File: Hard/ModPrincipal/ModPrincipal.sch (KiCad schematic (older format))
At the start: 0 parts

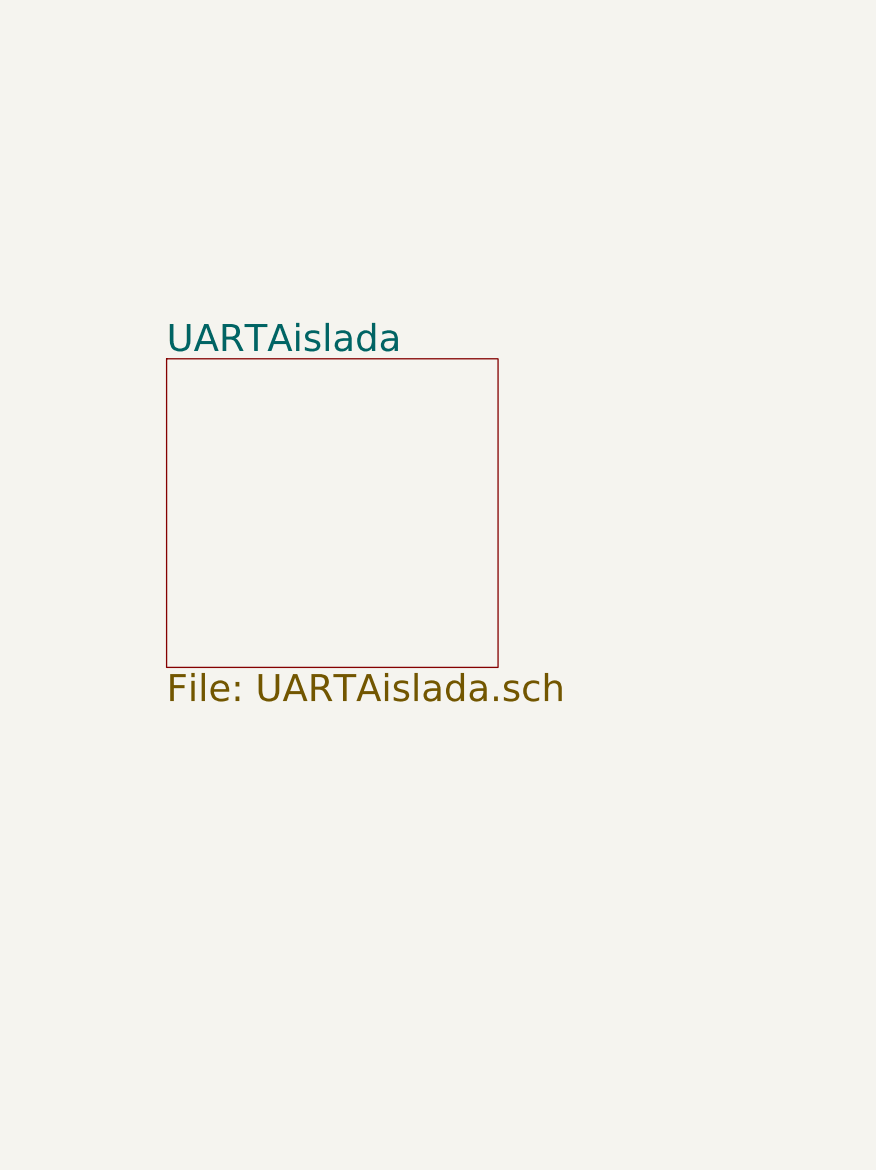
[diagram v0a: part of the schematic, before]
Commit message: Agrego UART aislada y salidas digitales
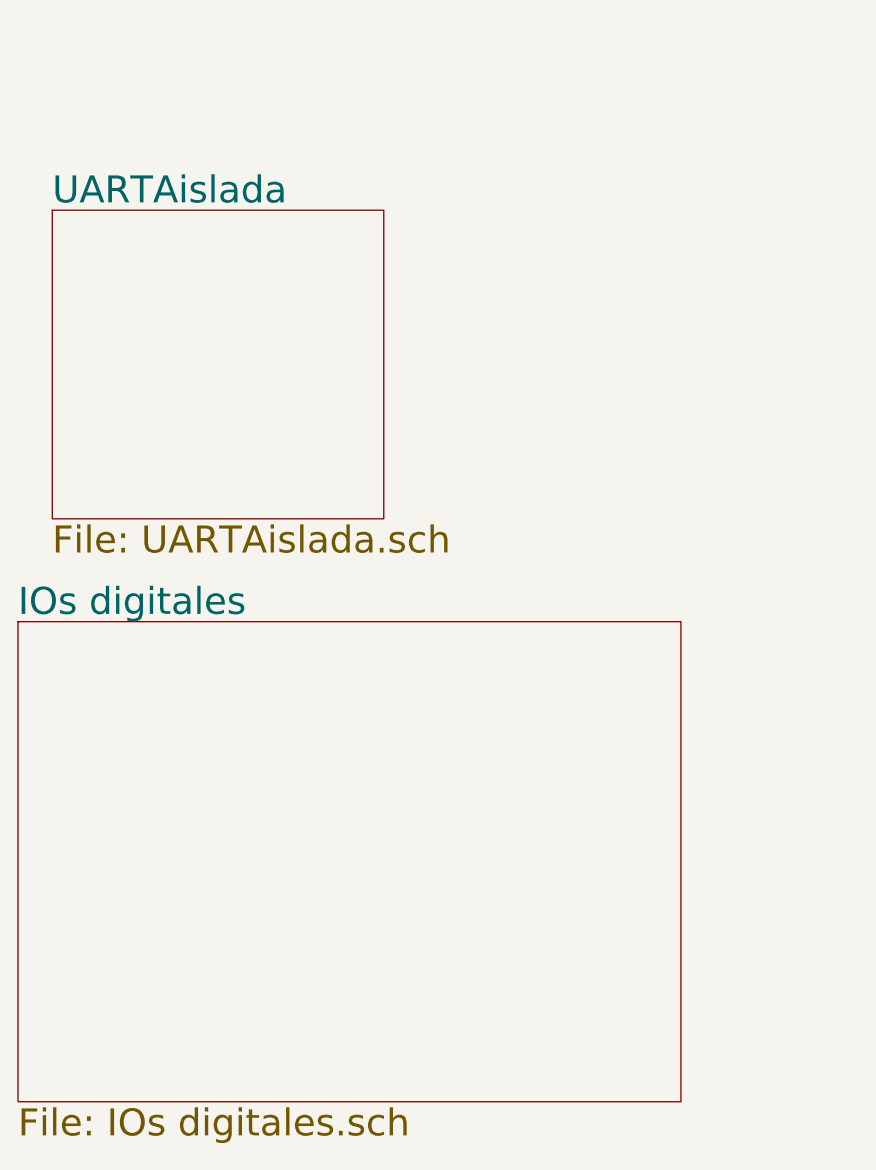
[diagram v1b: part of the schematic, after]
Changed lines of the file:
@@
 EESchema Schematic File Version 4
-LIBS:ModPrincipal-cache
 EELAYER 30 0
 EELAYER END
 $Descr A4 11693 8268
 encoding utf-8
-Sheet 1 4
+Sheet 1 5
 Title ""
 Date ""
@@
 $EndSheet
 $Sheet
-S 2150 4100 1450 1350
+S 1650 3450 1450 1350
 U 5ED20EE2
 F0 "UARTAislada" 118
 F1 "UARTAislada.sch" 118
 $EndSheet
+$Sheet
+S 1500 5250 2900 2100
+U 5EE6B2B0
+F0 "IOs digitales" 118
+F1 "IOs digitales.sch" 118
+$EndSheet
 $EndSCHEMATC

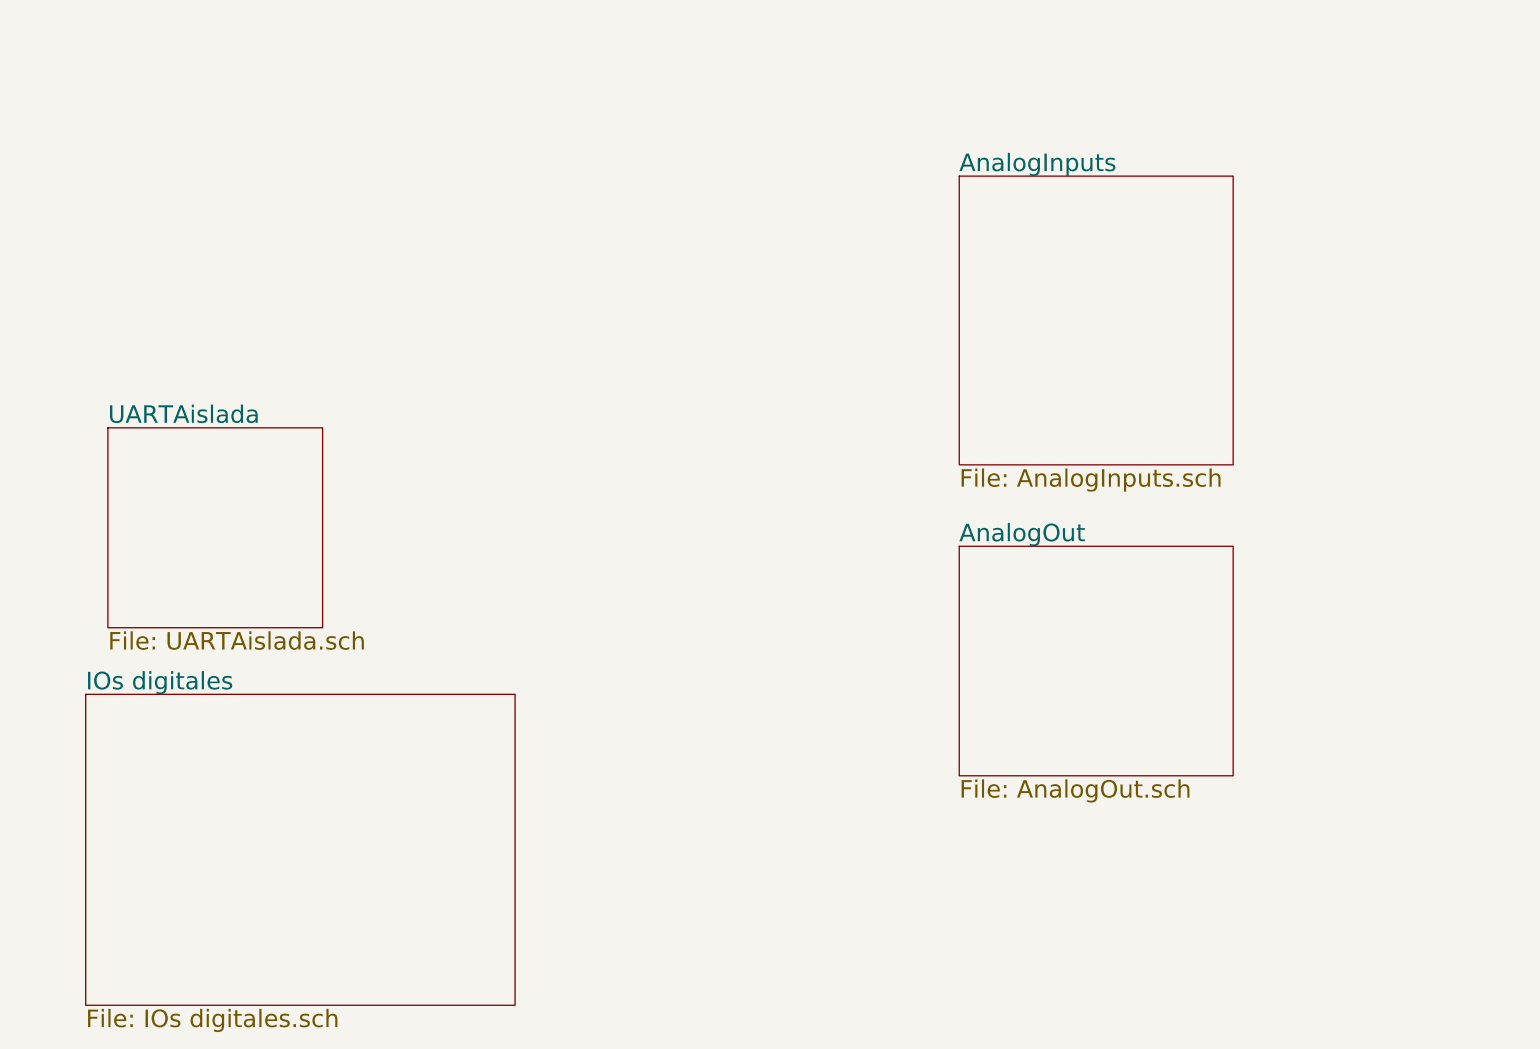
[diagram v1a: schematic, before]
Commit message: Agrego fuente de alimentación
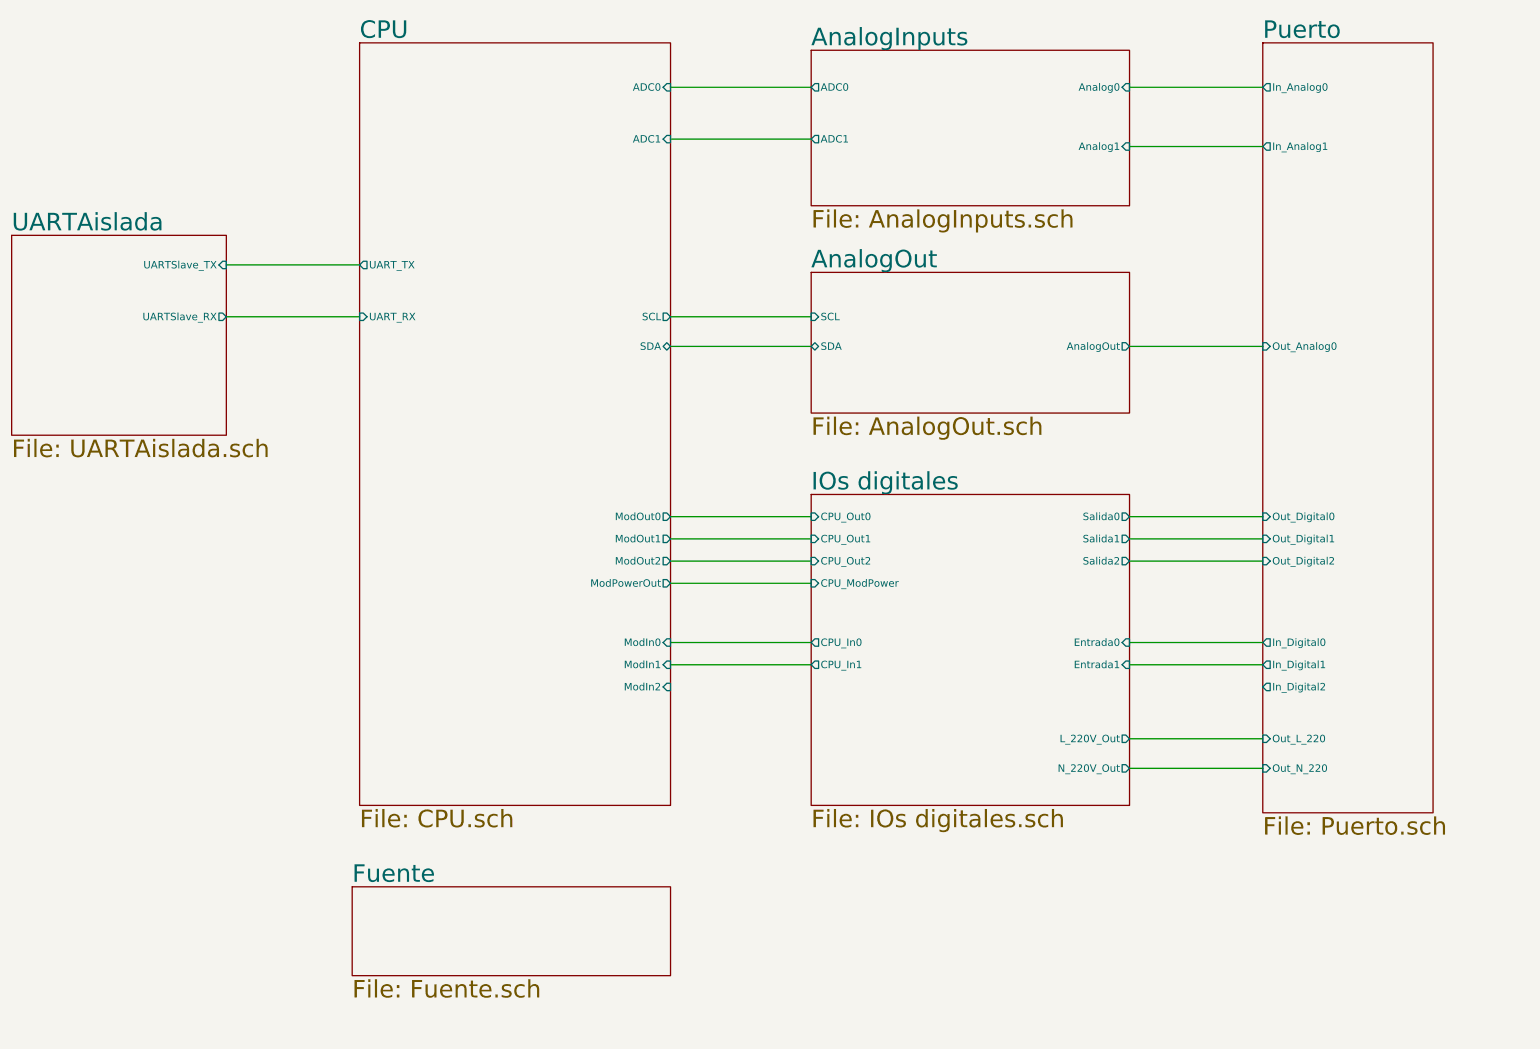
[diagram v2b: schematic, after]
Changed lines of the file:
@@
 $Descr A4 11693 8268
 encoding utf-8
-Sheet 1 5
+Sheet 1 8
 Title ""
 Date ""
@@
 $EndDescr
 $Sheet
-S 7400 1750 1850 1950
+S 6400 900  2150 1050
 U 5EC7150D
 F0 "AnalogInputs" 118
 F1 "AnalogInputs.sch" 118
+F2 "Analog0" I R 8550 1150 50
+F3 "Analog1" I R 8550 1550 50
+F4 "ADC0" O L 6400 1150 50
+F5 "ADC1" O L 6400 1500 50
 $EndSheet
 $Sheet
-S 7400 4250 1850 1550
+S 6400 2400 2150 950
 U 5ECD8445
 F0 "AnalogOut" 118
 F1 "AnalogOut.sch" 118
+F2 "AnalogOut" O R 8550 2900 50
+F3 "SDA" B L 6400 2900 50
+F4 "SCL" I L 6400 2700 50
 $EndSheet
 $Sheet
-S 1650 3450 1450 1350
+S 1000 2150 1450 1350
 U 5ED20EE2
 F0 "UARTAislada" 118
 F1 "UARTAislada.sch" 118
+F2 "UARTSlave_TX" I R 2450 2350 50
+F3 "UARTSlave_RX" O R 2450 2700 50
 $EndSheet
 $Sheet
-S 1500 5250 2900 2100
+S 3300 6550 2150 600
+U 5ECEE31C
+F0 "Fuente" 118
+F1 "Fuente.sch" 118
+$EndSheet
+Wire Wire Line
+	3350 2350 2450 2350
+Wire Wire Line
+	2450 2700 3350 2700
+$Sheet
+S 9450 850  1150 5200
+U 5EE56CB1
+F0 "Puerto" 118
+F1 "Puerto.sch" 118
+F2 "Out_Digital1" I L 9450 4200 50
+F3 "Out_Digital2" I L 9450 4350 50
+F4 "Out_Digital0" I L 9450 4050 50
+F5 "In_Digital1" O L 9450 5050 50
+F6 "In_Digital2" O L 9450 5200 50
+F7 "In_Digital0" O L 9450 4900 50
+F8 "Out_Analog0" I L 9450 2900 50
+F9 "In_Analog0" O L 9450 1150 50
+F10 "In_Analog1" O L 9450 1550 50
+F11 "Out_L_220" I L 9450 5550 50
+F12 "Out_N_220" I L 9450 5750 50
+$EndSheet
+Wire Wire Line
+	8550 1150 9450 1150
+Wire Wire Line
+	9450 1550 8550 1550
+Wire Wire Line
+	8550 2900 9450 2900
+$Sheet
+S 6400 3900 2150 2100
 U 5EE6B2B0
 F0 "IOs digitales" 118
 F1 "IOs digitales.sch" 118
+F2 "CPU_Out0" I L 6400 4050 50
+F3 "CPU_Out1" I L 6400 4200 50
+F4 "CPU_Out2" I L 6400 4350 50
+F5 "Salida0" O R 8550 4050 50
+F6 "Salida1" O R 8550 4200 50
+F7 "Salida2" O R 8550 4350 50
+F8 "CPU_In0" O L 6400 4900 50
+F9 "Entrada0" I R 8550 4900 50
+F10 "CPU_In1" O L 6400 5050 50
+F11 "Entrada1" I R 8550 5050 50
+F12 "CPU_ModPower" I L 6400 4500 50
+F13 "L_220V_Out" O R 8550 5550 50
+F14 "N_220V_Out" O R 8550 5750 50
 $EndSheet
+Wire Wire Line
+	8550 4050 9450 4050
+Wire Wire Line
+	9450 4200 8550 4200
+Wire Wire Line
+	8550 4350 9450 4350
+Wire Wire Line
+	8550 4900 9450 4900
+Wire Wire Line
+	9450 5050 8550 5050
+Wire Wire Line
+	8550 5550 9450 5550
+Wire Wire Line
+	8550 5750 9450 5750
+$Sheet
+S 3350 850  2100 5150
+U 5ED9C9D6
+F0 "CPU" 118
+F1 "CPU.sch" 118
+F2 "ADC0" I R 5450 1150 50
+F3 "ADC1" I R 5450 1500 50
+F4 "UART_RX" I L 3350 2700 50
+F5 "UART_TX" O L 3350 2350 50
+F6 "ModPowerOut" O R 5450 4500 50
+F7 "ModOut0" O R 5450 4050 50
+F8 "ModOut1" O R 5450 4200 50
+F9 "ModOut2" O R 5450 4350 50
+F10 "ModIn0" I R 5450 4900 50
+F11 "ModIn1" I R 5450 5050 50
+F12 "ModIn2" I R 5450 5200 50
+F13 "SCL" O R 5450 2700 50
+F14 "SDA" B R 5450 2900 50
+$EndSheet
+Wire Wire Line
+	6400 1150 5450 1150
+Wire Wire Line
+	6400 1500 5450 1500
+Wire Wire Line
+	5450 2700 6400 2700
+Wire Wire Line
+	6400 2900 5450 2900
+Wire Wire Line
+	5450 4200 6400 4200
+Wire Wire Line
+	5450 4050 6400 4050
+Wire Wire Line
+	6400 4350 5450 4350
+Wire Wire Line
+	6400 4500 5450 4500
+Wire Wire Line
+	5450 4900 6400 4900
+Wire Wire Line
+	6400 5050 5450 5050
 $EndSCHEMATC

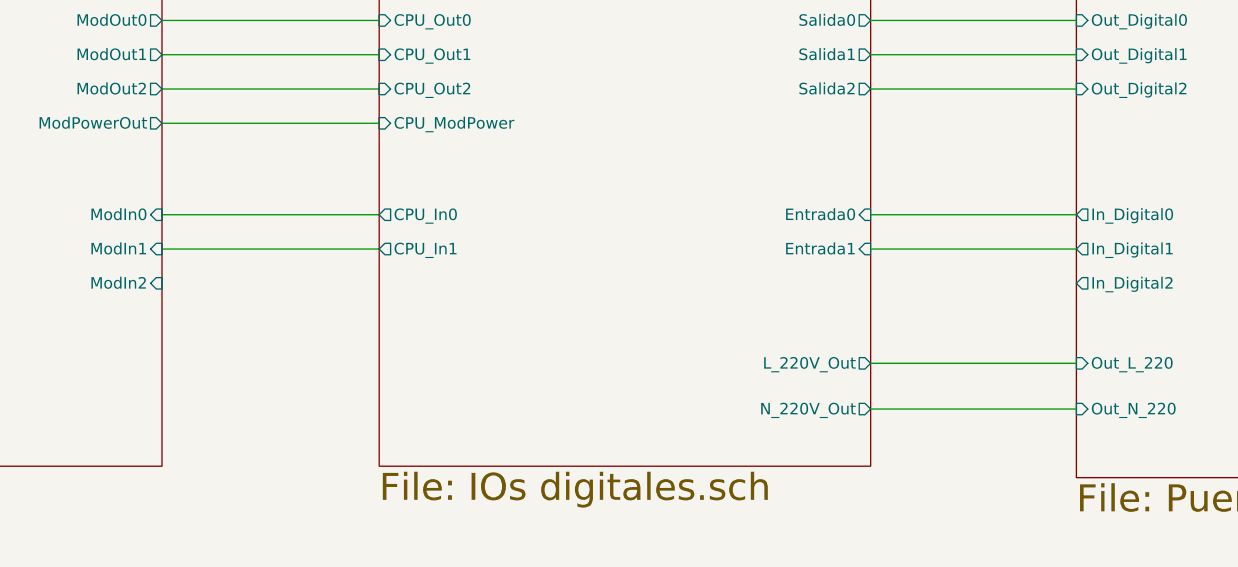
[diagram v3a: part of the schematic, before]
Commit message: Asignación de footprint y corrección de errores de ERC en esquematico
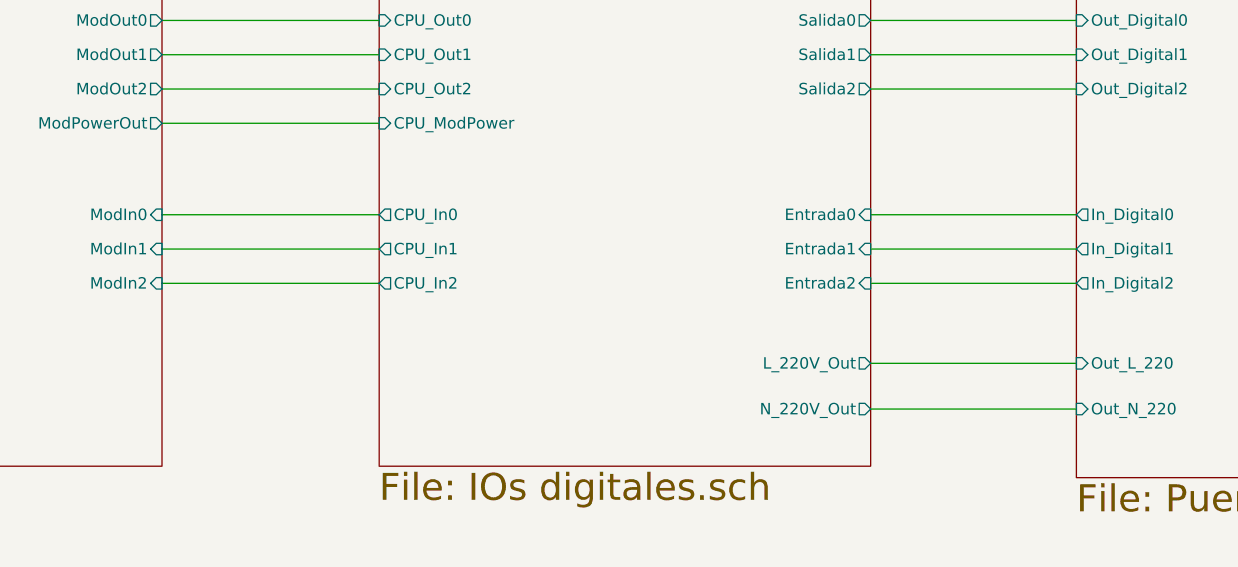
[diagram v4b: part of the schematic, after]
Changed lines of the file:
@@
 EESchema Schematic File Version 4
-LIBS:ModPrincipal-cache
 EELAYER 30 0
 EELAYER END
@@
 F13 "L_220V_Out" O R 8550 5550 50
 F14 "N_220V_Out" O R 8550 5750 50
+F15 "CPU_In2" O L 6400 5200 50
+F16 "Entrada2" I R 8550 5200 50
 $EndSheet
 Wire Wire Line
@@
 Wire Wire Line
 	6400 5050 5450 5050
+Wire Wire Line
+	9450 5200 8550 5200
+Wire Wire Line
+	6400 5200 5450 5200
 $EndSCHEMATC

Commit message: Inicio ubicacion de componentes
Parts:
- added H101, H102, H103, H104: MountingHole, MountingHole:MountingHole_3.2mm_M3, symbol Mechanical:MountingHole
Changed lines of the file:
@@
 EESchema Schematic File Version 4
+LIBS:ModPrincipal-cache
 EELAYER 30 0
 EELAYER END
@@
 Wire Wire Line
 	6400 5200 5450 5200
+$Comp
+L Mechanical:MountingHole H101
+U 1 1 5ED1215B
+P 1200 6450
+F 0 "H101" H 1300 6496 50  0000 L CNN
+F 1 "MountingHole" H 1300 6405 50  0000 L CNN
+F 2 "MountingHole:MountingHole_3.2mm_M3" H 1200 6450 50  0001 C CNN
+F 3 "~" H 1200 6450 50  0001 C CNN
+	1    1200 6450
+	1    0    0    -1
+$EndComp
+$Comp
+L Mechanical:MountingHole H103
+U 1 1 5ED12ABD
+P 1950 6450
+F 0 "H103" H 2050 6496 50  0000 L CNN
+F 1 "MountingHole" H 2050 6405 50  0000 L CNN
+F 2 "MountingHole:MountingHole_3.2mm_M3" H 1950 6450 50  0001 C CNN
+F 3 "~" H 1950 6450 50  0001 C CNN
+	1    1950 6450
+	1    0    0    -1
+$EndComp
+$Comp
+L Mechanical:MountingHole H102
+U 1 1 5ED130EC
+P 1200 6900
+F 0 "H102" H 1300 6946 50  0000 L CNN
+F 1 "MountingHole" H 1300 6855 50  0000 L CNN
+F 2 "MountingHole:MountingHole_3.2mm_M3" H 1200 6900 50  0001 C CNN
+F 3 "~" H 1200 6900 50  0001 C CNN
+	1    1200 6900
+	1    0    0    -1
+$EndComp
+$Comp
+L Mechanical:MountingHole H104
+U 1 1 5ED136EF
+P 1950 6900
+F 0 "H104" H 2050 6946 50  0000 L CNN
+F 1 "MountingHole" H 2050 6855 50  0000 L CNN
+F 2 "MountingHole:MountingHole_3.2mm_M3" H 1950 6900 50  0001 C CNN
+F 3 "~" H 1950 6900 50  0001 C CNN
+	1    1950 6900
+	1    0    0    -1
+$EndComp
 $EndSCHEMATC
